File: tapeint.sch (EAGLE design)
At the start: 20 parts, among them U1 MCP6241

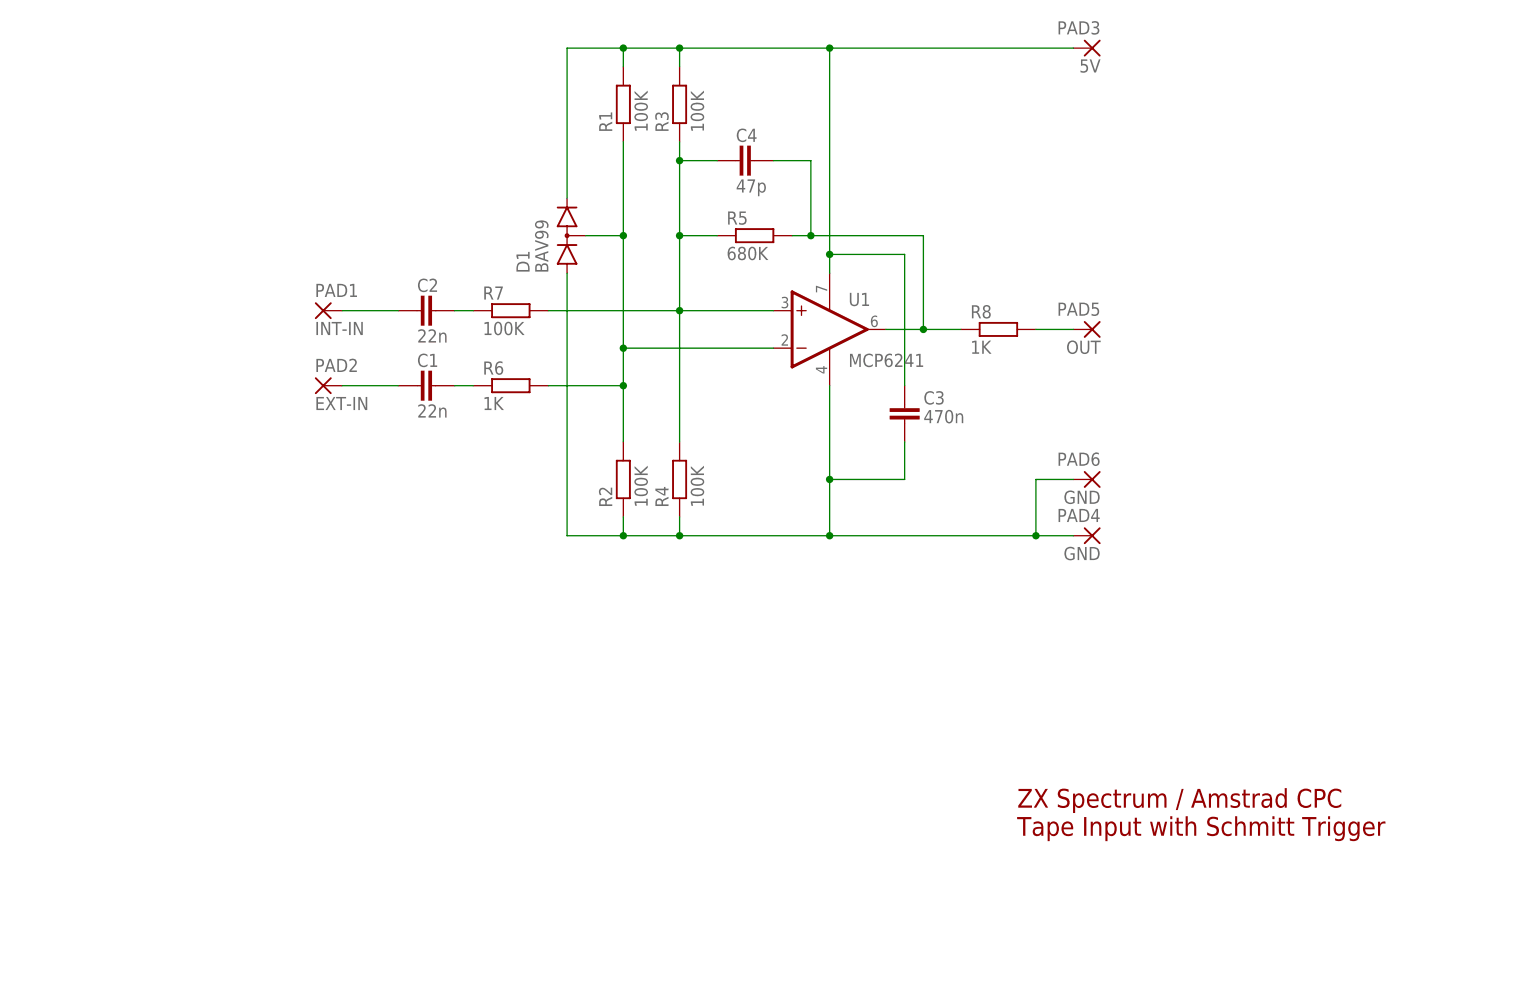
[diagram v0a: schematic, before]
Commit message: Updated version with better 0805 footprints, gerbers in a zip file, and BOM/CPL data for jlcpcb
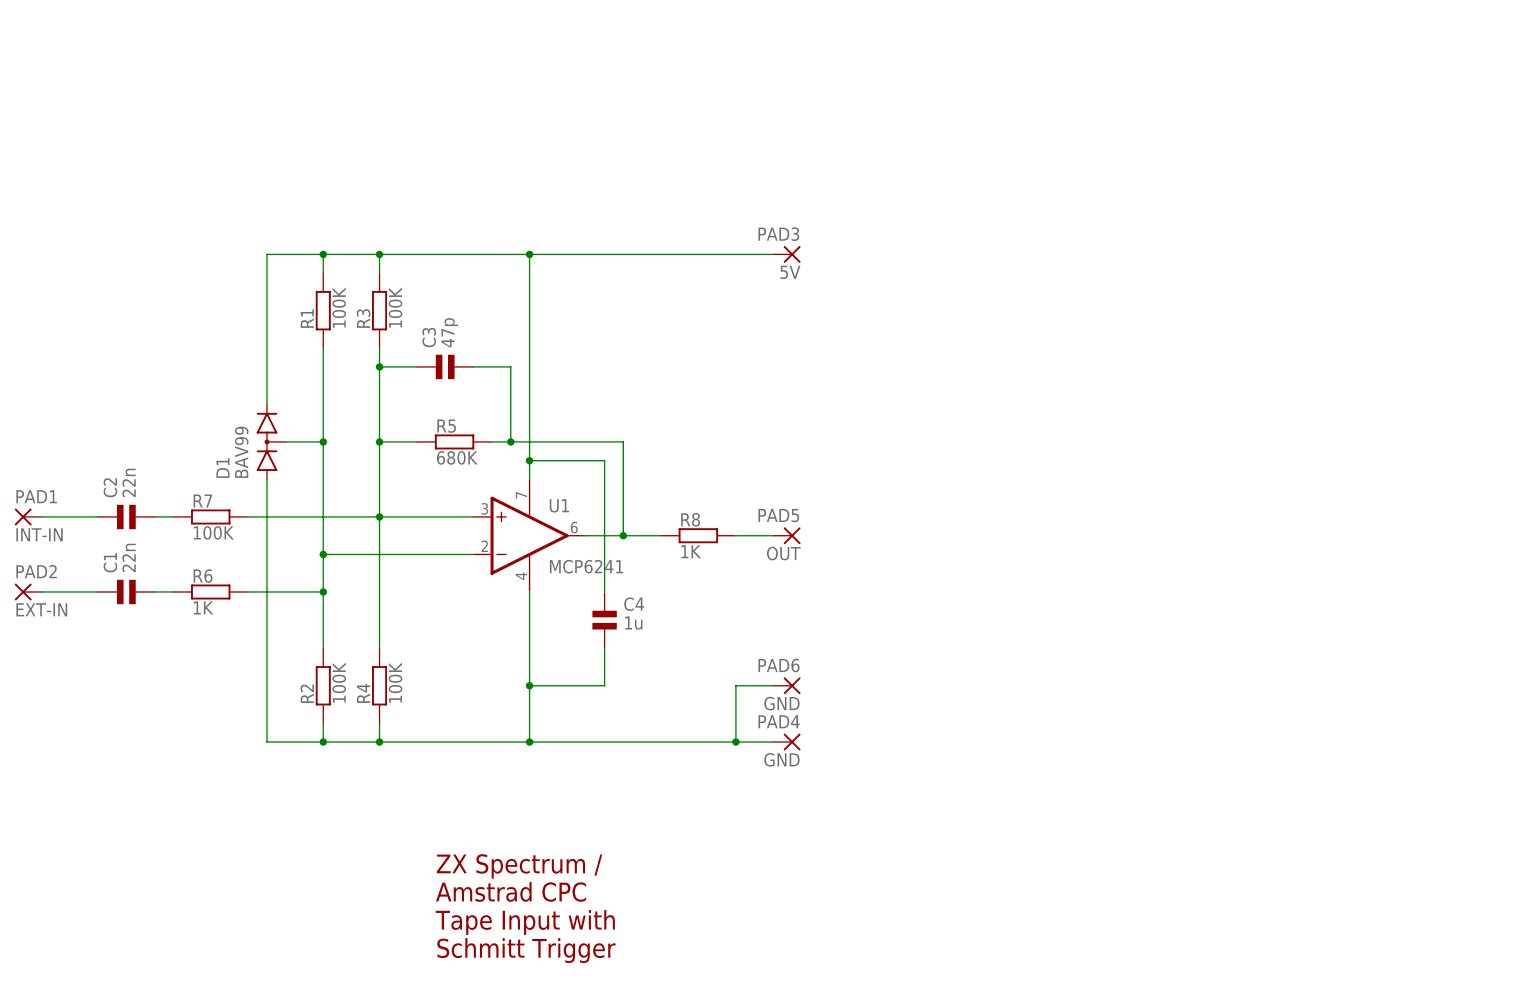
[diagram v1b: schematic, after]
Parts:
- C1, C2: device rcl:C-EUC0805 -> jc-passive:CAP_NPOL-0805
- C3: value 470n -> 47p; device rcl:C-EUC0805 -> jc-passive:CAP_NPOL-0805
- C4: value 47p -> 1u; device rcl:C-EUC0805 -> jc-passive:CAP_NPOL-0805
- R1, R2, R3, R4, R5, R6, R7, R8: device rcl:R-EU_R0805 -> jc-passive:RES-SMD_0805
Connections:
- net +5V: now also C4.1, D1.K2; no longer C3.1, D1.C
- net GND: now also C4.2, D1.A1; no longer C3.2, D1.A
- net N$3: now also D1.K1A2; no longer D1.AC
- net N$4: now also C3.1; no longer C4.1
- net OUT: now also C3.2; no longer C4.2
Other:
- moved on the sheet: D1, PAD1, PAD2, PAD3, PAD4, PAD5, PAD6, R1, R2, R3, R4, R5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
